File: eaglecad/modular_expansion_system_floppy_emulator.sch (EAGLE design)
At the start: 35 parts, among them IC1 74LS00N, IC11 74LS20N, IC2 74LS373N, IC3 74LS30N, IC4 74LS244N, IC5 74S74N, IC6 74LS139N, IC7 74LS155N, J1_ADDRESS_CON J1, J1_TEENSY_CON TEENSY_CON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

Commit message: all three boards designed
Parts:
- removed J3_WAIT_AND_INTERRUPT_BLOCK: J3, SparkFun-Connectors:CONN_20
- added J1-WAIT-AND-INT: WAIT-AND-INT, SparkFun-Connectors:CONN_04X2
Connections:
- removed net INT1*: J3_WAIT_AND_INTERRUPT_BLOCK.2
- removed net INT2*: J3_WAIT_AND_INTERRUPT_BLOCK.3
- removed net INT3*: J3_WAIT_AND_INTERRUPT_BLOCK.4
- removed net INT4*: J3_WAIT_AND_INTERRUPT_BLOCK.5
- removed net INT5*: J3_WAIT_AND_INTERRUPT_BLOCK.6
- removed net INT6*: J3_WAIT_AND_INTERRUPT_BLOCK.7
- removed net INT7*: J3_WAIT_AND_INTERRUPT_BLOCK.8
- removed net WAIT1*: J3_WAIT_AND_INTERRUPT_BLOCK.14
- removed net WAIT2*: J3_WAIT_AND_INTERRUPT_BLOCK.15
- removed net WAIT3*: J3_WAIT_AND_INTERRUPT_BLOCK.16
- removed net WAIT4*: J3_WAIT_AND_INTERRUPT_BLOCK.17
- removed net WAIT5*: J3_WAIT_AND_INTERRUPT_BLOCK.18
- removed net WAIT6*: J3_WAIT_AND_INTERRUPT_BLOCK.19
- removed net WAIT7*: J3_WAIT_AND_INTERRUPT_BLOCK.20
- net INT0*: now also J1-WAIT-AND-INT.1; no longer J3_WAIT_AND_INTERRUPT_BLOCK.1
- net WAIT0*: now also J1-WAIT-AND-INT.2; no longer J3_WAIT_AND_INTERRUPT_BLOCK.13
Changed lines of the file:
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@@
 <setting verticaltext="up"/>
 </settings>
-<grid distance="0.05" unitdist="inch" unit="inch" style="lines" multiple="1" display="no" altdistance="0.005" altunitdist="inch" altunit="inch"/>
+<grid distance="0.1" unitdist="inch" unit="inch" style="lines" multiple="1" display="no" altdistance="0.01" altunitdist="inch" altunit="inch"/>
 <layers>
 <layer number="1" name="Top" color="4" fill="1" visible="no" active="no"/>
@@
 <part name="GND8" library="supply1" library_urn="urn:adsk.eagle:library:371" deviceset="GND" device=""/>
 <part name="GND15" library="supply1" library_urn="urn:adsk.eagle:library:371" deviceset="GND" device=""/>
-<part name="J3_WAIT_AND_INTERRUPT_BLOCK" library="SparkFun-Connectors" library_urn="urn:adsk.eagle:library:513" deviceset="CONN_20" device="" package3d_urn="urn:adsk.eagle:package:38196/1" value="J3"/>
 <part name="J2_DATA_AND_POWER_CON" library="SparkFun-Connectors" library_urn="urn:adsk.eagle:library:513" deviceset="CONN_20" device="" package3d_urn="urn:adsk.eagle:package:38196/1" value="J2"/>
 <part name="J1_ADDRESS_CON" library="SparkFun-Connectors" library_urn="urn:adsk.eagle:library:513" deviceset="CONN_20" device="" package3d_urn="urn:adsk.eagle:package:38196/1" value="J1"/>
@@
 <part name="C8" library="rcl" library_urn="urn:adsk.eagle:library:334" deviceset="C-US" device="025-024X044" package3d_urn="urn:adsk.eagle:package:23630/1" value=".1uf"/>
 <part name="GND11" library="supply1" library_urn="urn:adsk.eagle:library:371" deviceset="GND" device=""/>
+<part name="J1-WAIT-AND-INT" library="SparkFun-Connectors" library_urn="urn:adsk.eagle:library:513" deviceset="CONN_04X2" device="" package3d_urn="urn:adsk.eagle:package:38103/1" value="WAIT-AND-INT"/>
 </parts>
 <sheets>
@@
 <attribute name="VALUE" x="194.31" y="27.94" size="1.778" layer="96" rot="R90"/>
 </instance>
-<instance part="J3_WAIT_AND_INTERRUPT_BLOCK" gate="G$1" x="-124.46" y="-27.94" smashed="yes">
-<attribute name="VALUE" x="-124.46" y="-27.686" size="1.778" layer="96" font="vector"/>
-<attribute name="NAME" x="-122.428" y="-17.78" size="1.778" layer="95" font="vector" rot="R90"/>
-</instance>
 <instance part="J2_DATA_AND_POWER_CON" gate="G$1" x="-78.74" y="137.16" smashed="yes" rot="R270">
 <attribute name="VALUE" x="-78.486" y="137.16" size="1.778" layer="96" font="vector" rot="R270"/>
@@
 <instance part="GND11" gate="1" x="143.51" y="82.55" smashed="yes" rot="R270">
 <attribute name="VALUE" x="140.97" y="85.09" size="1.778" layer="96" rot="R270"/>
+</instance>
+<instance part="J1-WAIT-AND-INT" gate="G$1" x="-119.38" y="-12.7" smashed="yes">
+<attribute name="VALUE" x="-123.19" y="-20.066" size="1.778" layer="96" font="vector"/>
+<attribute name="NAME" x="-123.444" y="-4.572" size="1.778" layer="95" font="vector"/>
 </instance>
 </instances>
@@
 <label x="-38.1" y="116.84" size="1.778" layer="95"/>
 <wire x1="-12.7" y1="119.38" x2="-12.7" y2="101.6" width="0.762" layer="92"/>
-</segment>
-</bus>
-<bus name="INTERRUPT_AND_WAIT:INT0*,INT1*,INT2*,INT3*,INT4*,INT5*,INT6*,INT7*,WAIT0*,WAIT1*,WAIT2*,WAIT3*,WAIT4*,WAIT5*,WAIT6*,WAIT7*">
-<segment>
-<wire x1="-106.68" y1="-22.86" x2="-106.68" y2="25.4" width="0.762" layer="92"/>
 </segment>
 </bus>
@@
 <net name="INT0*" class="0">
 <segment>
-<pinref part="J3_WAIT_AND_INTERRUPT_BLOCK" gate="G$1" pin="1"/>
-<wire x1="-106.68" y1="-22.86" x2="-114.3" y2="-22.86" width="0.1524" layer="91"/>
-</segment>
-<segment>
-<wire x1="-106.68" y1="-2.54" x2="180.34" y2="-2.54" width="0.1524" layer="91"/>
+<wire x1="-127" y1="-2.54" x2="180.34" y2="-2.54" width="0.1524" layer="91"/>
 <label x="86.36" y="-2.032" size="1.016" layer="95"/>
 <label x="-105.41" y="-2.032" size="1.016" layer="95"/>
@@
 <wire x1="180.34" y1="-55.88" x2="205.74" y2="-55.88" width="0.1524" layer="91"/>
 <label x="190.5" y="-55.88" size="1.016" layer="95"/>
-</segment>
-</net>
-<net name="INT1*" class="0">
-<segment>
-<pinref part="J3_WAIT_AND_INTERRUPT_BLOCK" gate="G$1" pin="2"/>
-<wire x1="-106.68" y1="-20.32" x2="-114.3" y2="-20.32" width="0.1524" layer="91"/>
-</segment>
-</net>
-<net name="INT2*" class="0">
-<segment>
-<pinref part="J3_WAIT_AND_INTERRUPT_BLOCK" gate="G$1" pin="3"/>
-<wire x1="-106.68" y1="-17.78" x2="-114.3" y2="-17.78" width="0.1524" layer="91"/>
-</segment>
-</net>
-<net name="INT3*" class="0">
-<segment>
-<pinref part="J3_WAIT_AND_INTERRUPT_BLOCK" gate="G$1" pin="4"/>
-<wire x1="-106.68" y1="-15.24" x2="-114.3" y2="-15.24" width="0.1524" layer="91"/>
-</segment>
-</net>
-<net name="INT4*" class="0">
-<segment>
-<pinref part="J3_WAIT_AND_INTERRUPT_BLOCK" gate="G$1" pin="5"/>
-<wire x1="-106.68" y1="-12.7" x2="-114.3" y2="-12.7" width="0.1524" layer="91"/>
-</segment>
-</net>
-<net name="INT5*" class="0">
-<segment>
-<pinref part="J3_WAIT_AND_INTERRUPT_BLOCK" gate="G$1" pin="6"/>
-<wire x1="-106.68" y1="-10.16" x2="-114.3" y2="-10.16" width="0.1524" layer="91"/>
-</segment>
-</net>
-<net name="INT6*" class="0">
-<segment>
-<pinref part="J3_WAIT_AND_INTERRUPT_BLOCK" gate="G$1" pin="7"/>
-<wire x1="-106.68" y1="-7.62" x2="-114.3" y2="-7.62" width="0.1524" layer="91"/>
-</segment>
-</net>
-<net name="INT7*" class="0">
-<segment>
-<pinref part="J3_WAIT_AND_INTERRUPT_BLOCK" gate="G$1" pin="8"/>
-<wire x1="-106.68" y1="-5.08" x2="-114.3" y2="-5.08" width="0.1524" layer="91"/>
+<pinref part="J1-WAIT-AND-INT" gate="G$1" pin="1"/>
+<wire x1="-127" y1="-7.62" x2="-127" y2="-2.54" width="0.1524" layer="91"/>
 </segment>
 </net>
 <net name="WAIT0*" class="0">
-<segment>
-<pinref part="J3_WAIT_AND_INTERRUPT_BLOCK" gate="G$1" pin="13"/>
-<wire x1="-106.68" y1="7.62" x2="-114.3" y2="7.62" width="0.1524" layer="91"/>
-</segment>
 <segment>
 <pinref part="IC5" gate="A" pin="!Q"/>
@@
 <label x="111.76" y="10.16" size="1.016" layer="95"/>
 <label x="-105.41" y="3.048" size="1.016" layer="95"/>
-</segment>
-</net>
-<net name="WAIT1*" class="0">
-<segment>
-<pinref part="J3_WAIT_AND_INTERRUPT_BLOCK" gate="G$1" pin="14"/>
-<wire x1="-106.68" y1="10.16" x2="-114.3" y2="10.16" width="0.1524" layer="91"/>
-</segment>
-</net>
-<net name="WAIT2*" class="0">
-<segment>
-<pinref part="J3_WAIT_AND_INTERRUPT_BLOCK" gate="G$1" pin="15"/>
-<wire x1="-106.68" y1="12.7" x2="-114.3" y2="12.7" width="0.1524" layer="91"/>
-</segment>
-</net>
-<net name="WAIT3*" class="0">
-<segment>
-<pinref part="J3_WAIT_AND_INTERRUPT_BLOCK" gate="G$1" pin="16"/>
-<wire x1="-106.68" y1="15.24" x2="-114.3" y2="15.24" width="0.1524" layer="91"/>
-</segment>
-</net>
-<net name="WAIT4*" class="0">
-<segment>
-<pinref part="J3_WAIT_AND_INTERRUPT_BLOCK" gate="G$1" pin="17"/>
-<wire x1="-106.68" y1="17.78" x2="-114.3" y2="17.78" width="0.1524" layer="91"/>
-</segment>
-</net>
-<net name="WAIT5*" class="0">
-<segment>
-<pinref part="J3_WAIT_AND_INTERRUPT_BLOCK" gate="G$1" pin="18"/>
-<wire x1="-106.68" y1="20.32" x2="-114.3" y2="20.32" width="0.1524" layer="91"/>
-</segment>
-</net>
-<net name="WAIT6*" class="0">
-<segment>
-<pinref part="J3_WAIT_AND_INTERRUPT_BLOCK" gate="G$1" pin="19"/>
-<wire x1="-106.68" y1="22.86" x2="-114.3" y2="22.86" width="0.1524" layer="91"/>
-</segment>
-</net>
-<net name="WAIT7*" class="0">
-<segment>
-<pinref part="J3_WAIT_AND_INTERRUPT_BLOCK" gate="G$1" pin="20"/>
-<wire x1="-106.68" y1="25.4" x2="-114.3" y2="25.4" width="0.1524" layer="91"/>
-</segment>
-</net>
+<pinref part="J1-WAIT-AND-INT" gate="G$1" pin="2"/>
+<wire x1="-111.76" y1="-7.62" x2="-106.68" y2="-7.62" width="0.1524" layer="91"/>
+<wire x1="-106.68" y1="-7.62" x2="-106.68" y2="2.54" width="0.1524" layer="91"/>
+</segment>
+</net>

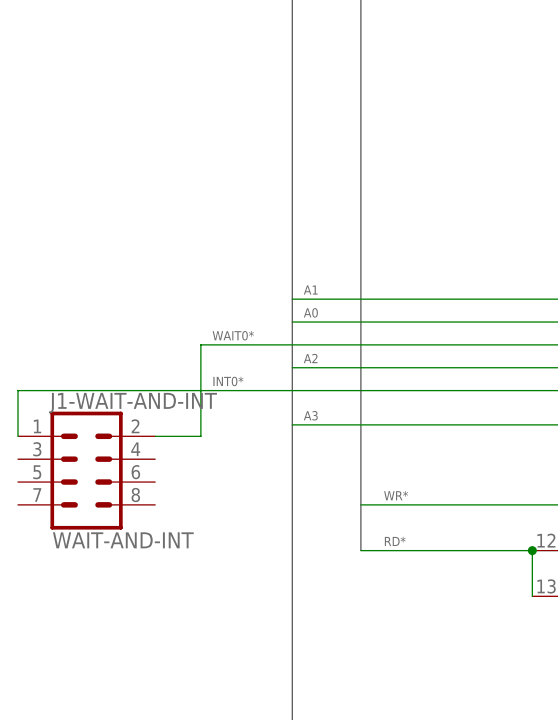
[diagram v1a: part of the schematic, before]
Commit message: removed soft reset for vdp, added 12 voice sound
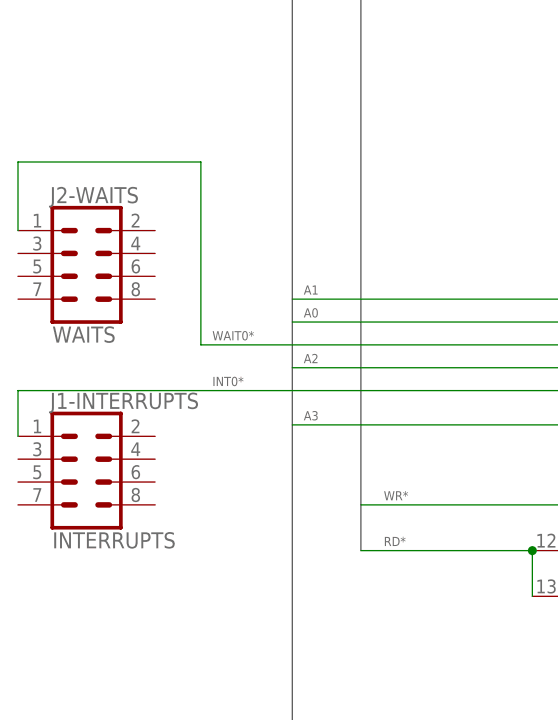
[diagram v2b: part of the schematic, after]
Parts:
- added J2-WAITS: WAITS, SparkFun-Connectors:CONN_04X2
- J1-INTERRUPTS: value WAIT-AND-INT -> INTERRUPTS
- renumbered J1-WAIT-AND-INT to J1-INTERRUPTS
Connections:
- net WAIT0*: now also J2-WAITS.1; no longer J1-INTERRUPTS.2
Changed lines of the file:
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@@
 <part name="C8" library="rcl" library_urn="urn:adsk.eagle:library:334" deviceset="C-US" device="025-024X044" package3d_urn="urn:adsk.eagle:package:23630/1" value=".1uf"/>
 <part name="GND11" library="supply1" library_urn="urn:adsk.eagle:library:371" deviceset="GND" device=""/>
-<part name="J1-WAIT-AND-INT" library="SparkFun-Connectors" library_urn="urn:adsk.eagle:library:513" deviceset="CONN_04X2" device="" package3d_urn="urn:adsk.eagle:package:38103/1" value="WAIT-AND-INT"/>
+<part name="J1-INTERRUPTS" library="SparkFun-Connectors" library_urn="urn:adsk.eagle:library:513" deviceset="CONN_04X2" device="" package3d_urn="urn:adsk.eagle:package:38103/1" value="INTERRUPTS"/>
+<part name="J2-WAITS" library="SparkFun-Connectors" library_urn="urn:adsk.eagle:library:513" deviceset="CONN_04X2" device="" package3d_urn="urn:adsk.eagle:package:38103/1" value="WAITS"/>
 </parts>
 <sheets>
@@
 <attribute name="VALUE" x="140.97" y="85.09" size="1.778" layer="96" rot="R270"/>
 </instance>
-<instance part="J1-WAIT-AND-INT" gate="G$1" x="-119.38" y="-12.7" smashed="yes">
+<instance part="J1-INTERRUPTS" gate="G$1" x="-119.38" y="-12.7" smashed="yes">
 <attribute name="VALUE" x="-123.19" y="-20.066" size="1.778" layer="96" font="vector"/>
 <attribute name="NAME" x="-123.444" y="-4.572" size="1.778" layer="95" font="vector"/>
+</instance>
+<instance part="J2-WAITS" gate="G$1" x="-119.38" y="10.16" smashed="yes">
+<attribute name="VALUE" x="-123.19" y="2.794" size="1.778" layer="96" font="vector"/>
+<attribute name="NAME" x="-123.444" y="18.288" size="1.778" layer="95" font="vector"/>
 </instance>
 </instances>
@@
 <wire x1="180.34" y1="-55.88" x2="205.74" y2="-55.88" width="0.1524" layer="91"/>
 <label x="190.5" y="-55.88" size="1.016" layer="95"/>
-<pinref part="J1-WAIT-AND-INT" gate="G$1" pin="1"/>
+<pinref part="J1-INTERRUPTS" gate="G$1" pin="1"/>
 <wire x1="-127" y1="-7.62" x2="-127" y2="-2.54" width="0.1524" layer="91"/>
 </segment>
@@
 <label x="111.76" y="10.16" size="1.016" layer="95"/>
 <label x="-105.41" y="3.048" size="1.016" layer="95"/>
-<pinref part="J1-WAIT-AND-INT" gate="G$1" pin="2"/>
-<wire x1="-111.76" y1="-7.62" x2="-106.68" y2="-7.62" width="0.1524" layer="91"/>
-<wire x1="-106.68" y1="-7.62" x2="-106.68" y2="2.54" width="0.1524" layer="91"/>
-</segment>
-</net>
+<pinref part="J2-WAITS" gate="G$1" pin="1"/>
+<wire x1="-127" y1="15.24" x2="-127" y2="22.86" width="0.1524" layer="91"/>
+<wire x1="-127" y1="22.86" x2="-106.68" y2="22.86" width="0.1524" layer="91"/>
+<wire x1="-106.68" y1="22.86" x2="-106.68" y2="2.54" width="0.1524" layer="91"/>
+</segment>
+</net>

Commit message: bug in the base board RD, WR, IN, and OUT signals
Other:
- moved on the sheet: IC1C
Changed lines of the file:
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@@
 <attribute name="VALUE" x="-63.5" y="118.11" size="1.778" layer="96"/>
 </instance>
-<instance part="IC1" gate="C" x="196.85" y="113.03" smashed="yes">
-<attribute name="NAME" x="189.23" y="118.745" size="1.778" layer="95"/>
-<attribute name="VALUE" x="189.23" y="105.41" size="1.778" layer="96"/>
-</instance>
-<instance part="GND9" gate="1" x="184.15" y="97.79" smashed="yes">
-<attribute name="VALUE" x="181.61" y="95.25" size="1.778" layer="96"/>
+<instance part="IC1" gate="C" x="199.39" y="148.59" smashed="yes">
+<attribute name="NAME" x="191.77" y="154.305" size="1.778" layer="95"/>
+<attribute name="VALUE" x="191.77" y="140.97" size="1.778" layer="96"/>
+</instance>
+<instance part="GND9" gate="1" x="186.69" y="133.35" smashed="yes">
+<attribute name="VALUE" x="184.15" y="130.81" size="1.778" layer="96"/>
 </instance>
 <instance part="P+3" gate="VCC" x="-80.01" y="130.81" smashed="yes">
@@
 <pinref part="IC1" gate="C" pin="I0"/>
 <pinref part="IC1" gate="C" pin="I1"/>
-<wire x1="184.15" y1="115.57" x2="184.15" y2="110.49" width="0.1524" layer="91"/>
+<wire x1="186.69" y1="151.13" x2="186.69" y2="146.05" width="0.1524" layer="91"/>
 <pinref part="GND9" gate="1" pin="GND"/>
-<wire x1="184.15" y1="110.49" x2="184.15" y2="100.33" width="0.1524" layer="91"/>
-<junction x="184.15" y="110.49"/>
-</segment>
-<segment>
+<wire x1="186.69" y1="146.05" x2="186.69" y2="135.89" width="0.1524" layer="91"/>
+<junction x="186.69" y="146.05"/>
+</segment>
+<segment>

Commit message: Fixes for mount, stand alond joystick boards, level shifters Adafruit
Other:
- moved on the sheet: IC3, IC6A
